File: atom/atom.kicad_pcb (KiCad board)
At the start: 2 copper layers, 109 x 54 mm, 64 parts, among them J10 TC2030_NL, J101 MALE, J1010 MALE, J102 FEMALE, J103 MALE, J1030 MALE, J104 FEMALE, J105 MALE, J1050 MALE, J106 FEMALE, J107 MALE, J1070 MALE, J108 FEMALE, J11 STANDOFF, J111 STANDOFF, J112 STANDOFF, J113 STANDOFF, J114 STANDOFF, J12 STANDOFF, J13 STANDOFF, J14 STANDOFF, J2 FEMALE, J4 FEMALE, J6 FEMALE, J8 FEMALE, J9 DTR, Q1 2N3904, SW1 ACTION, SW2 ACTION, SW3 ACTION, SW4 ACTION, U3 ATmega328P-MU, Y1 YSX321SL

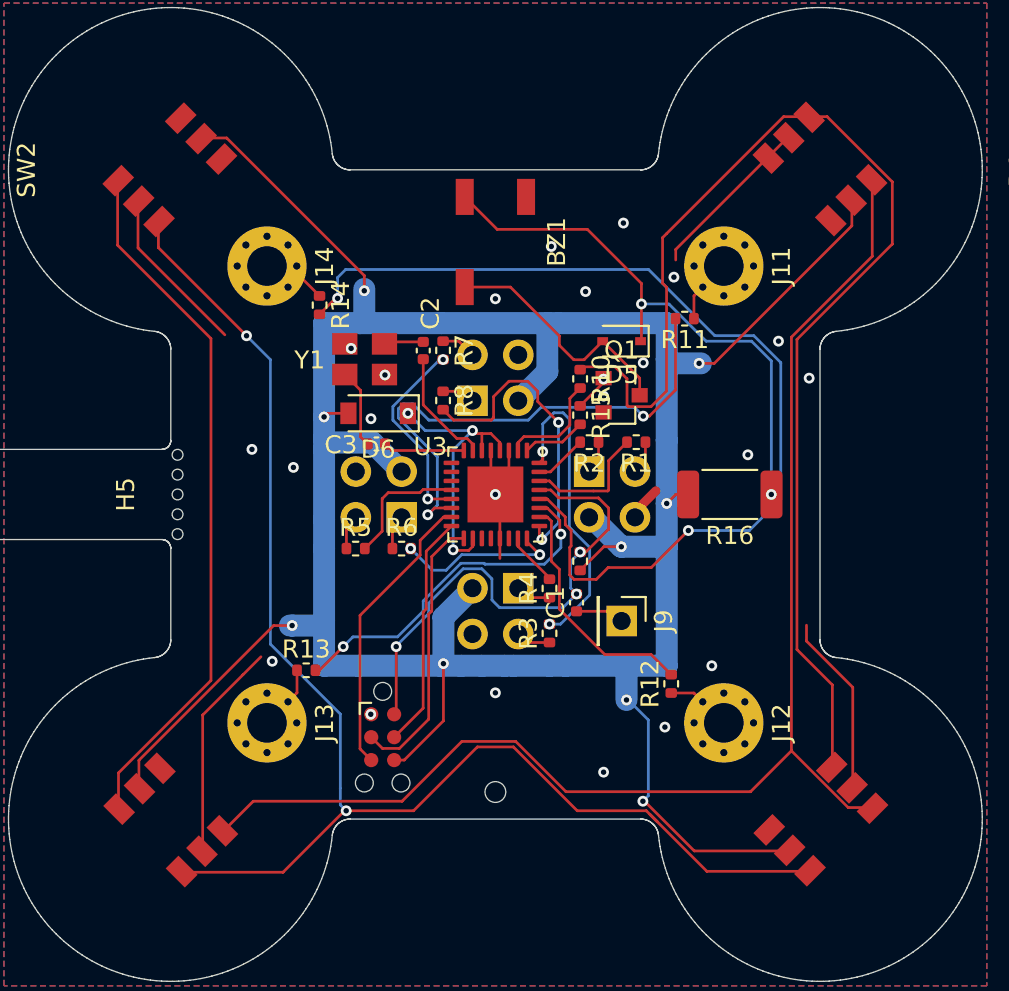
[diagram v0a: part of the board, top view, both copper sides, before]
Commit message: Reroute to accommodate larger clearance
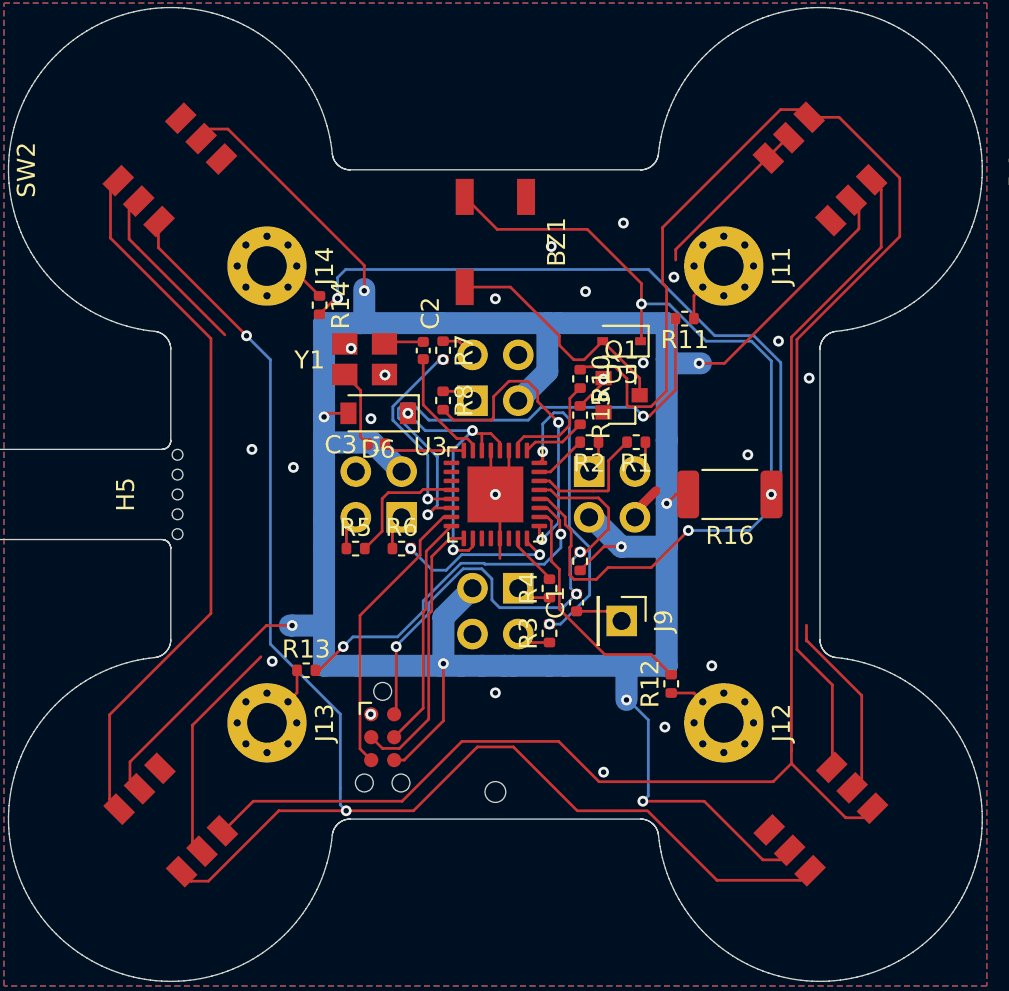
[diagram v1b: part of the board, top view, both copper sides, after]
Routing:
- net +5VB: track 172.7 -> 175.5 mm
- net GNDB: track 52.4 -> 53.8 mm
- net /Lower Board/DIN: track 68.0 -> 69.4 mm
- net Net-(D3-Pad3): track 39.0 -> 39.9 mm
- net Net-(D1-Pad3): track 75.0 -> 75.6 mm
